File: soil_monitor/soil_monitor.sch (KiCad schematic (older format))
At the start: 6 parts, among them IC1 ATTINY13A-P, P1 CONN_01X03, SW1 SW_PUSH

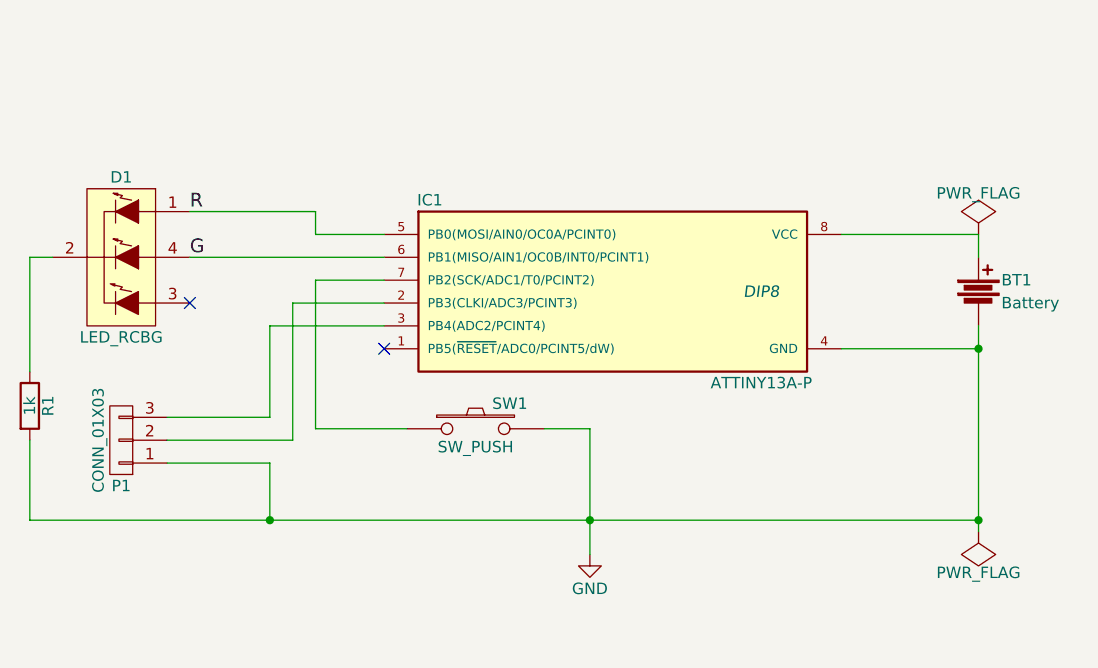
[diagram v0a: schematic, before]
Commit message: Changed pin assignment for R and G pin. Updated code to slow down warning interval, and also for a clearer good to dry colour spectrum. Also, since ADC uses internal 1.1V reference and the sensor output gives 4.2V, so resistor divider is used (3k and 1k)
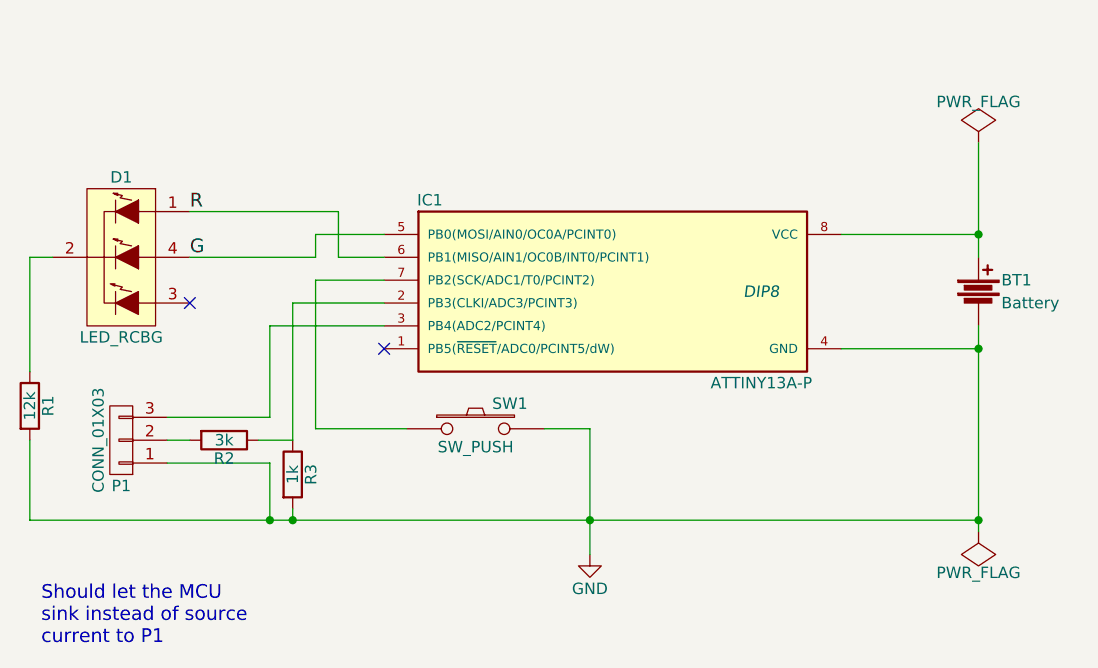
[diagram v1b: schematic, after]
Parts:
- added R2: 3k, symbol R
- added R3: 1k, symbol R
- R1: value 1k -> 12k
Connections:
- net G: now also IC1.5 (PB0(MOSI/AIN0/OC0A/PCINT0)); no longer IC1.6 (PB1(MISO/AIN1/OC0B/INT0/PCINT1))
- net GND: now also R3.2
- net R: now also IC1.6 (PB1(MISO/AIN1/OC0B/INT0/PCINT1)); no longer IC1.5 (PB0(MOSI/AIN0/OC0A/PCINT0))
- net at IC1.2 (PB3(CLKI/ADC3/PCINT3)): now also R2.1, R3.1; no longer P1.2 (P2)
- new net: P1.2 (P2), R2.2
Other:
- note added: "Should let the MCU \nsink instead of source \ncurrent to P1"
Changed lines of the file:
@@
 $EndComp
 Wire Wire Line
-	6350 3000 6350 2900
+	6350 2500 6350 3000
 Wire Wire Line
 	6350 2900 5750 2900
@@
 $EndComp
 Wire Wire Line
-	2800 3800 3350 3800
-Wire Wire Line
-	3350 3800 3350 3200
-Wire Wire Line
 	3350 3200 3750 3200
 Wire Wire Line
@@
 $EndComp
 Wire Wire Line
-	3750 3000 2900 3000
-Wire Wire Line
-	2900 2800 3450 2800
-Wire Wire Line
-	3450 2800 3450 2900
-Wire Wire Line
-	3450 2900 3750 2900
-Wire Wire Line
 	2300 3000 2200 3000
 Wire Wire Line
@@
 L PWR_FLAG #FLG1
 U 1 1 5A9C7B5D
-P 6350 2900
-F 0 "#FLG1" H 6350 2995 50  0001 C CNN
-F 1 "PWR_FLAG" H 6350 3080 50  0000 C CNN
-F 2 "" H 6350 2900 50  0000 C CNN
-F 3 "" H 6350 2900 50  0000 C CNN
-	1    6350 2900
+P 6350 2500
+F 0 "#FLG1" H 6350 2595 50  0001 C CNN
+F 1 "PWR_FLAG" H 6350 2680 50  0000 C CNN
+F 2 "" H 6350 2500 50  0000 C CNN
+F 3 "" H 6350 2500 50  0000 C CNN
+	1    6350 2500
 	1    0    0    -1
 $EndComp
@@
 P 2200 3650
 F 0 "R1" V 2280 3650 50  0000 C CNN
-F 1 "1k" V 2200 3650 50  0000 C CNN
+F 1 "12k" V 2200 3650 50  0000 C CNN
 F 2 "" V 2130 3650 50  0000 C CNN
 F 3 "" H 2200 3650 50  0000 C CNN
@@
 Wire Wire Line
 	2200 4150 2200 3800
+Wire Wire Line
+	3750 2900 3450 2900
+Wire Wire Line
+	3450 2900 3450 3000
+Wire Wire Line
+	3450 3000 2900 3000
+Wire Wire Line
+	3750 3000 3550 3000
+Wire Wire Line
+	3550 3000 3550 2800
+Wire Wire Line
+	3550 2800 2900 2800
+$Comp
+L R R2
+U 1 1 5AB78E02
+P 3050 3800
+F 0 "R2" V 3130 3800 50  0000 C CNN
+F 1 "3k" V 3050 3800 50  0000 C CNN
+F 2 "" V 2980 3800 50  0000 C CNN
+F 3 "" H 3050 3800 50  0000 C CNN
+	1    3050 3800
+	0    1    1    0
+$EndComp
+$Comp
+L R R3
+U 1 1 5AB78EB6
+P 3350 3950
+F 0 "R3" V 3430 3950 50  0000 C CNN
+F 1 "1k" V 3350 3950 50  0000 C CNN
+F 2 "" V 3280 3950 50  0000 C CNN
+F 3 "" H 3350 3950 50  0000 C CNN
+	1    3350 3950
+	1    0    0    -1
+$EndComp
+Wire Wire Line
+	3350 3200 3350 3800
+Wire Wire Line
+	3350 3800 3200 3800
+Wire Wire Line
+	2900 3800 2800 3800
+Wire Wire Line
+	3350 4100 3350 4150
+Connection ~ 3350 4150
+Connection ~ 6350 2900
+Text Notes 2250 4700 0    60   ~ 0
+Should let the MCU \nsink instead of source \ncurrent to P1
 $EndSCHEMATC

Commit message: MCU no longer sourcing the sensor, but sinking instead.
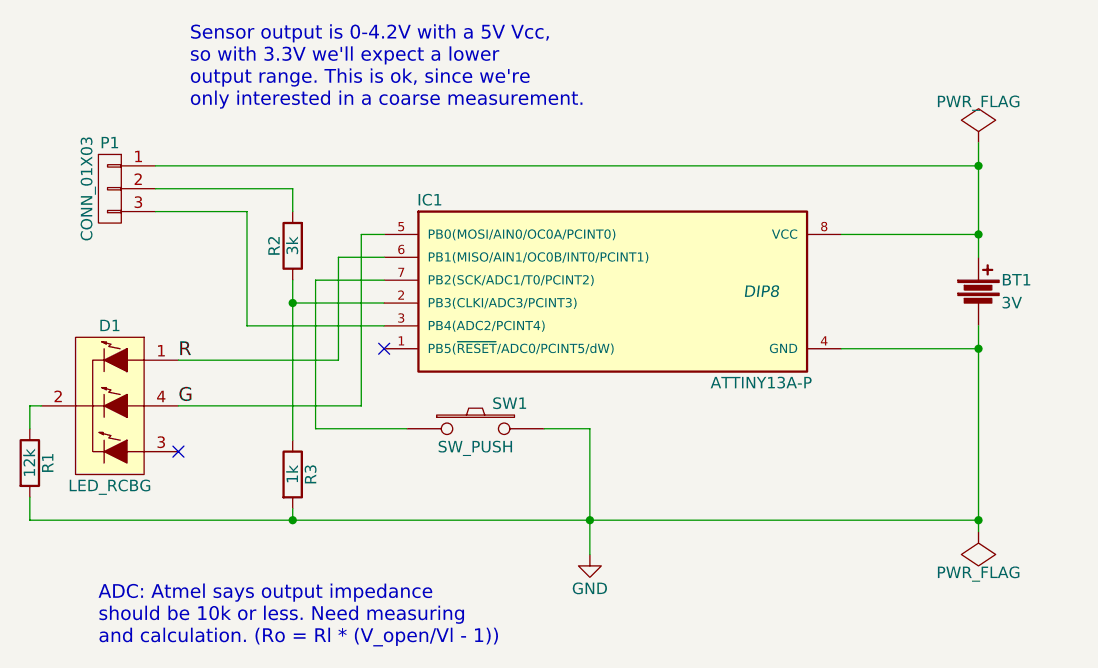
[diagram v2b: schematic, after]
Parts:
- BT1: value Battery -> 3V
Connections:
- net GND: no longer P1.1 (P1)
- net at BT1.1, IC1.8 (VCC): now also P1.1 (P1)
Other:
- note added: "ADC: Atmel says output impedance \nshould be 10k or less. Need measuring\nand calculation. (Ro = Rl * (V_open/Vl - 1))"
- note added: "Sensor output is 0-4.2V with a 5V Vcc, \nso with 3.3V we'll expect a lower \noutput range. This is ok, since we're \nonly interested in a coarse measurement."
- note removed: "Should let the MCU \nsink instead of source \ncurrent to P1"
- moved on the sheet: D1, P1, R1, R2
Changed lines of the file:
@@
 P 6350 3150
 F 0 "BT1" H 6450 3200 50  0000 L CNN
-F 1 "Battery" H 6450 3100 50  0000 L CNN
+F 1 "3V" H 6450 3100 50  0000 L CNN
 F 2 "" V 6350 3190 50  0000 C CNN
 F 3 "" V 6350 3190 50  0000 C CNN
@@
 L CONN_01X03 P1
 U 1 1 5A9C7399
-P 2600 3800
-F 0 "P1" H 2600 4000 50  0000 C CNN
-F 1 "CONN_01X03" V 2700 3800 50  0000 C CNN
-F 2 "" H 2600 3800 50  0000 C CNN
-F 3 "" H 2600 3800 50  0000 C CNN
-	1    2600 3800
-	-1   0    0    1
+P 2550 2700
+F 0 "P1" H 2550 2900 50  0000 C CNN
+F 1 "CONN_01X03" V 2650 2700 50  0000 C CNN
+F 2 "" H 2550 2700 50  0000 C CNN
+F 3 "" H 2550 2700 50  0000 C CNN
+	1    2550 2700
+	-1   0    0    -1
 $EndComp
 Wire Wire Line
 	3350 3200 3750 3200
-Wire Wire Line
-	3750 3300 3250 3300
-Wire Wire Line
-	3250 3300 3250 3700
-Wire Wire Line
-	3250 3700 2800 3700
 $Comp
 L LED_RCBG D1
 U 1 1 5A9C7471
-P 2600 3000
-F 0 "D1" H 2600 3350 50  0000 C CNN
-F 1 "LED_RCBG" H 2600 2650 50  0000 C CNN
-F 2 "" H 2600 2950 50  0000 C CNN
-F 3 "" H 2600 2950 50  0000 C CNN
-	1    2600 3000
+P 2550 3650
+F 0 "D1" H 2550 4000 50  0000 C CNN
+F 1 "LED_RCBG" H 2550 3300 50  0000 C CNN
+F 2 "" H 2550 3600 50  0000 C CNN
+F 3 "" H 2550 3600 50  0000 C CNN
+	1    2550 3650
 	1    0    0    -1
 $EndComp
 Wire Wire Line
-	2300 3000 2200 3000
-Wire Wire Line
 	2200 4150 6350 4150
 Connection ~ 4650 4150
-NoConn ~ 2900 3200
+NoConn ~ 2850 3850
 NoConn ~ 3750 3400
 $Comp
@@
 $EndComp
 Connection ~ 6350 4150
-Wire Wire Line
-	2800 3900 3250 3900
-Wire Wire Line
-	3250 3900 3250 4150
-Connection ~ 3250 4150
-Text Label 2900 2800 0    60   ~ 0
+Text Label 2850 3450 0    60   ~ 0
 R
-Text Label 2900 3000 0    60   ~ 0
+Text Label 2850 3650 0    60   ~ 0
 G
 $Comp
 L R R1
 U 1 1 5A9C7EA0
-P 2200 3650
-F 0 "R1" V 2280 3650 50  0000 C CNN
-F 1 "12k" V 2200 3650 50  0000 C CNN
-F 2 "" V 2130 3650 50  0000 C CNN
-F 3 "" H 2200 3650 50  0000 C CNN
-	1    2200 3650
+P 2200 3900
+F 0 "R1" V 2280 3900 50  0000 C CNN
+F 1 "12k" V 2200 3900 50  0000 C CNN
+F 2 "" V 2130 3900 50  0000 C CNN
+F 3 "" H 2200 3900 50  0000 C CNN
+	1    2200 3900
 	1    0    0    -1
 $EndComp
-Wire Wire Line
-	2200 3000 2200 3500
-Wire Wire Line
-	2200 4150 2200 3800
-Wire Wire Line
-	3750 2900 3450 2900
-Wire Wire Line
-	3450 2900 3450 3000
-Wire Wire Line
-	3450 3000 2900 3000
-Wire Wire Line
-	3750 3000 3550 3000
-Wire Wire Line
-	3550 3000 3550 2800
-Wire Wire Line
-	3550 2800 2900 2800
 $Comp
 L R R2
 U 1 1 5AB78E02
-P 3050 3800
-F 0 "R2" V 3130 3800 50  0000 C CNN
-F 1 "3k" V 3050 3800 50  0000 C CNN
-F 2 "" V 2980 3800 50  0000 C CNN
-F 3 "" H 3050 3800 50  0000 C CNN
-	1    3050 3800
-	0    1    1    0
+P 3350 2950
+F 0 "R2" V 3430 2950 50  0000 C CNN
+F 1 "3k" V 3350 2950 50  0000 C CNN
+F 2 "" V 3280 2950 50  0000 C CNN
+F 3 "" H 3350 2950 50  0000 C CNN
+	1    3350 2950
+	-1   0    0    1
 $EndComp
 $Comp
@@
 $EndComp
 Wire Wire Line
-	3350 3200 3350 3800
-Wire Wire Line
-	3350 3800 3200 3800
-Wire Wire Line
-	2900 3800 2800 3800
+	3350 3100 3350 3800
 Wire Wire Line
 	3350 4100 3350 4150
 Connection ~ 3350 4150
 Connection ~ 6350 2900
-Text Notes 2250 4700 0    60   ~ 0
-Should let the MCU \nsink instead of source \ncurrent to P1
+Wire Wire Line
+	2250 3650 2200 3650
+Wire Wire Line
+	3150 3300 3750 3300
+Wire Wire Line
+	3350 2800 3350 2700
+Wire Wire Line
+	3350 2700 2750 2700
+Wire Wire Line
+	2750 2800 3150 2800
+Wire Wire Line
+	3150 2800 3150 3300
+Connection ~ 3350 3200
+Wire Wire Line
+	2750 2600 6350 2600
+Connection ~ 6350 2600
+Wire Wire Line
+	3750 3000 3550 3000
+Wire Wire Line
+	3550 3000 3550 3450
+Wire Wire Line
+	3550 3450 2850 3450
+Wire Wire Line
+	3750 2900 3650 2900
+Wire Wire Line
+	3650 2900 3650 3650
+Wire Wire Line
+	3650 3650 2850 3650
+Wire Wire Line
+	2200 4050 2200 4150
+Wire Wire Line
+	2200 3650 2200 3750
+Text Notes 2500 4700 0    60   ~ 0
+ADC: Atmel says output impedance \nshould be 10k or less. Need measuring\nand calculation. (Ro = Rl * (V_open/Vl - 1))
+Text Notes 2900 2350 0    60   ~ 0
+Sensor output is 0-4.2V with a 5V Vcc, \nso with 3.3V we'll expect a lower \noutput range. This is ok, since we're \nonly interested in a coarse measurement.
 $EndSCHEMATC
